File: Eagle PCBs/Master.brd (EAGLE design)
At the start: 56.8 x 35.6 mm, 9 parts

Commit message: Master PCB WIP
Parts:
- moved R1 27.9 mm to (26.7, 11.4), turned to 90 degrees
- moved C3 26.2 mm to (29.2, 2.54), turned to 180 degrees
- moved RS485-MASTER 18.1 mm to (34.3, 10.2), turned to 90 degrees
- moved 5V-VRR 17.0 mm to (39.4, 26.7), turned to 270 degrees
- moved C2 11.7 mm to (25.4, 20.3), turned to 180 degrees
- moved MEGA 4.02 mm to (44.5, 10.2), turned to 90 degrees
- moved C1 2.84 mm to (24.1, 30.5), turned to 90 degrees
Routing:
- net RS485_A: track 80.0 -> 21.3 mm
- net RS485_B: track 62.0 -> 22.8 mm
- net VCC12: track 44.2 -> 30.5 mm
- net VCC: track 39.8 -> 41.6 mm
- net GND: track 4.16 -> 4.72 mm
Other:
- board size 56.8 x 35.6 mm -> 53 x 35.6 mm

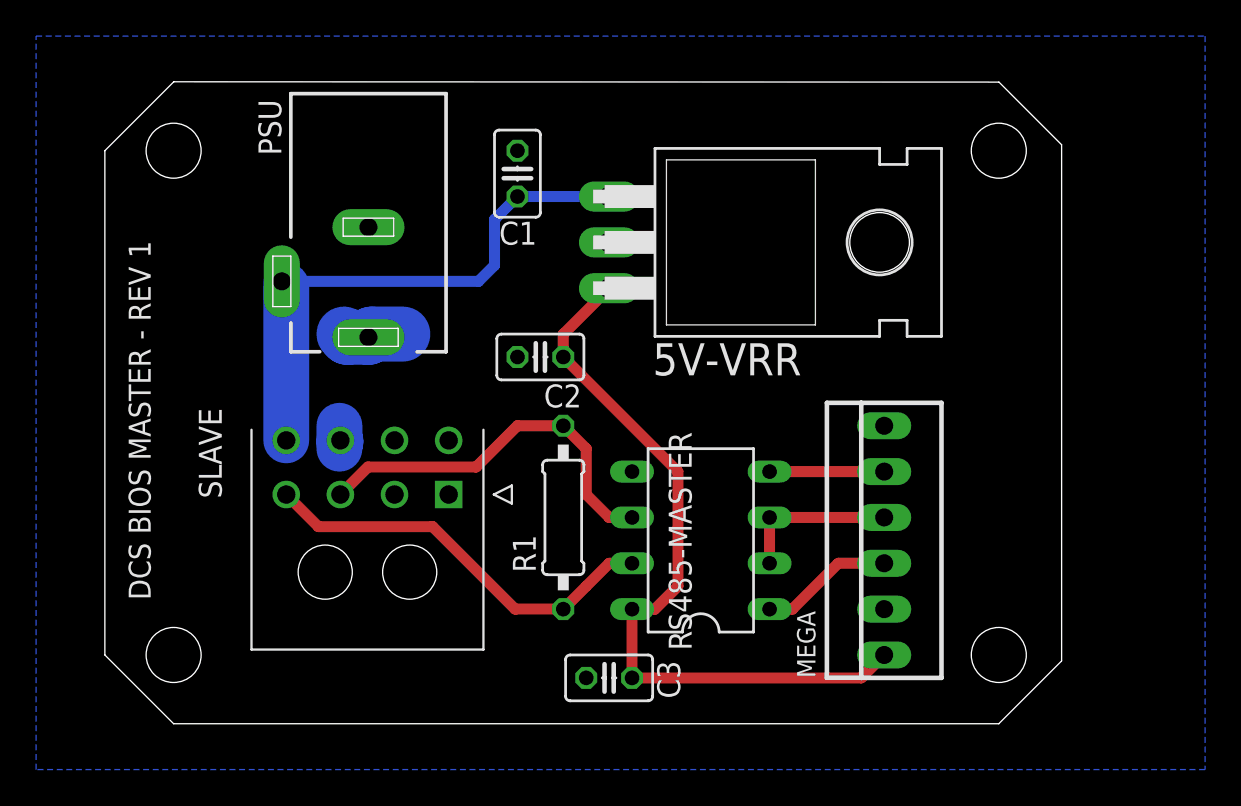
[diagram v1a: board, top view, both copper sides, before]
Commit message: Updated DC Barrel Jack
DC-044A
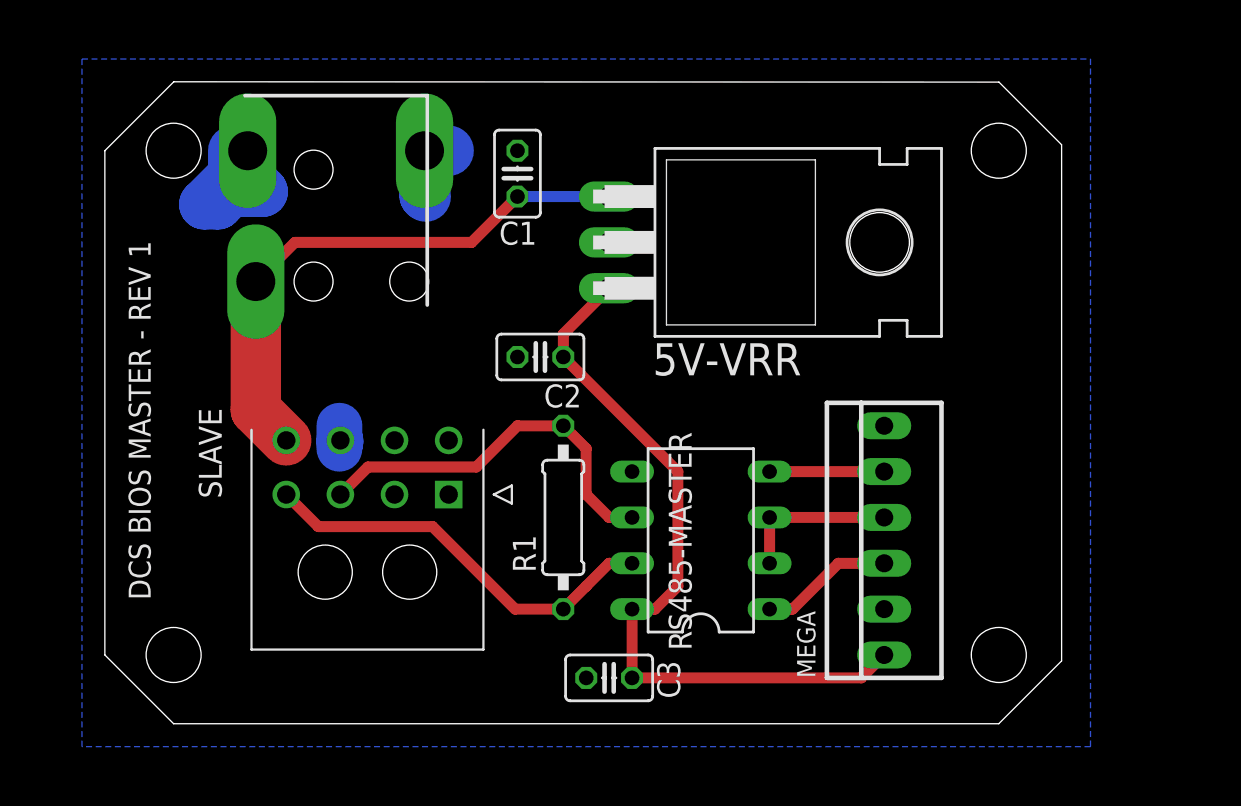
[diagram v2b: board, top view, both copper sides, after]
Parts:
- removed PSU: 12VDC C+, con-jack:DCJ0202
- added U$1: DC-044A, A10 Library:DC-044A
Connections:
- net GND: now also U$1.GND, U$1.GND-2; no longer PSU.1
- net VCC12: now also U$1.1; no longer PSU.2
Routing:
- net GND: track 4.72 -> 15.0 mm
- net VCC12: track 30.5 -> 31.0 mm
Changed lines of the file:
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@@
 <attribute name="VALUE" x="36.195" y="5.334" size="1.27" layer="27" ratio="10" rot="R90"/>
-</element>
-<element name="PSU" library="con-jack" library_urn="urn:adsk.eagle:library:154" package="DCJ0202" package3d_urn="urn:adsk.eagle:package:7491/1" value="12VDC C+" x="15.875" y="24.511" smashed="yes" rot="R180">
-<attribute name="MF" value="" x="-3.175" y="35.941" size="1.778" layer="27" rot="R180" display="off"/>
-<attribute name="MPN" value="" x="-3.175" y="35.941" size="1.778" layer="27" rot="R180" display="off"/>
-<attribute name="NAME" x="11.049" y="31.496" size="1.27" layer="25" rot="R90"/>
-<attribute name="OC_FARNELL" value="unknown" x="-3.175" y="35.941" size="1.778" layer="27" rot="R180" display="off"/>
-<attribute name="OC_NEWARK" value="unknown" x="-3.175" y="35.941" size="1.778" layer="27" rot="R180" display="off"/>
-<attribute name="POPULARITY" value="17" x="-3.175" y="35.941" size="1.778" layer="27" rot="R180" display="off"/>
-<attribute name="VALUE" x="20.574" y="35.179" size="1.27" layer="27" rot="R270"/>
 </element>
 <element name="MEGA" library="con-molex" library_urn="urn:adsk.eagle:library:165" package="22-23-2061" package3d_urn="urn:adsk.eagle:package:8078637/1" value="" x="44.45" y="10.16" smashed="yes" rot="R90">
@@
 <attribute name="VALUE" x="27.305" y="9.1694" size="1.27" layer="27" ratio="10" rot="R90"/>
 </element>
+<element name="U$1" library="A10 Library" package="DC-044A" value="DC-044A" x="14.053" y="28.28" smashed="yes" rot="R180">
+<attribute name="VALUE" x="19.133" y="22.819" size="1.27" layer="27" rot="R180"/>
+</element>
 </elements>
 <signals>
@@
 <contactref element="C1" pad="2"/>
 <contactref element="MEGA" pad="2"/>
-<contactref element="PSU" pad="1"/>
 <contactref element="C2" pad="2"/>
 <contactref element="C3" pad="2"/>
 <contactref element="SLAVE" pad="7"/>
 <polygon width="0.6096" layer="16" spacing="0.4064" isolate="0.4064">
-<vertex x="-2.54" y="38.1"/>
-<vertex x="62.23" y="38.1"/>
-<vertex x="62.23" y="-2.54"/>
-<vertex x="-2.54" y="-2.54"/>
+<vertex x="0" y="36.83"/>
+<vertex x="55.88" y="36.83"/>
+<vertex x="55.88" y="-1.27"/>
+<vertex x="0" y="-1.27"/>
 </polygon>
 <contactref element="RS485-MASTER" pad="5"/>
-<wire x1="15.875" y1="21.411" x2="16.054" y2="21.59" width="3.048" layer="16"/>
-<wire x1="16.054" y1="21.59" x2="17.78" y2="21.59" width="3.048" layer="16"/>
-<wire x1="15.875" y1="21.411" x2="14.6994" y2="21.411" width="3.048" layer="16"/>
-<wire x1="14.6994" y1="21.411" x2="14.5204" y2="21.59" width="3.048" layer="16"/>
 <wire x1="14.32" y1="15.7" x2="14.2664" y2="15.7536" width="2.54" layer="16"/>
 <wire x1="14.2664" y1="15.7536" x2="14.2664" y2="16.51" width="2.54" layer="16"/>
@@
 <wire x1="14.32" y1="15.59" x2="14.2664" y2="15.5364" width="2.54" layer="16"/>
 <wire x1="14.2664" y1="15.5364" x2="14.2664" y2="15.24" width="2.54" layer="16"/>
+<contactref element="U$1" pad="GND"/>
+<contactref element="U$1" pad="GND-2"/>
+<wire x1="18.983" y1="31.75" x2="20.32" y2="31.75" width="2.794" layer="16"/>
+<wire x1="18.983" y1="31.75" x2="18.983" y2="29.277" width="2.794" layer="16"/>
+<wire x1="18.983" y1="29.277" x2="19.05" y2="29.21" width="2.794" layer="16"/>
+<wire x1="9.183" y1="31.75" x2="9.183" y2="30.30888125" width="2.794" layer="16"/>
+<wire x1="9.183" y1="30.30888125" x2="10.01348125" y2="29.4784" width="2.794" layer="16"/>
+<wire x1="10.01348125" y1="29.4784" x2="8.2284375" y2="29.4784" width="2.794" layer="16"/>
+<wire x1="8.2284375" y1="29.4784" x2="7.53016875" y2="28.78013125" width="2.794" layer="16"/>
+<wire x1="7.53016875" y1="28.78013125" x2="6.77986875" y2="28.78013125" width="2.794" layer="16"/>
+<wire x1="6.77986875" y1="28.78013125" x2="8.382" y2="30.3822625" width="2.794" layer="16"/>
+<wire x1="8.382" y1="30.3822625" x2="8.382" y2="31.75" width="2.794" layer="16"/>
 </signal>
 <signal name="VCC12">
 <contactref element="5V-VRR" pad="1"/>
 <contactref element="C1" pad="1"/>
-<contactref element="PSU" pad="2"/>
 <wire x1="29.21" y1="29.21" x2="24.13" y2="29.21" width="0.6096" layer="16"/>
-<wire x1="24.13" y1="29.21" x2="22.86" y2="27.94" width="0.6096" layer="16"/>
-<wire x1="22.86" y1="27.94" x2="22.86" y2="25.4" width="0.6096" layer="16"/>
-<wire x1="22.86" y1="25.4" x2="21.971" y2="24.511" width="0.6096" layer="16"/>
-<wire x1="21.971" y1="24.511" x2="11.075" y2="24.511" width="0.6096" layer="16"/>
 <contactref element="SLAVE" pad="8"/>
-<wire x1="11.32" y1="24.266" x2="11.32" y2="15.7" width="2.54" layer="16"/>
-<wire x1="11.075" y1="24.511" x2="11.32" y2="24.266" width="2.032" layer="16"/>
+<contactref element="U$1" pad="1"/>
+<wire x1="9.633" y1="24.5" x2="9.633" y2="17.387" width="2.794" layer="1"/>
+<wire x1="9.633" y1="17.387" x2="11.32" y2="15.7" width="2.794" layer="1"/>
+<wire x1="9.633" y1="24.5" x2="11.803" y2="26.67" width="0.6096" layer="1"/>
+<wire x1="11.803" y1="26.67" x2="21.59" y2="26.67" width="0.6096" layer="1"/>
+<wire x1="21.59" y1="26.67" x2="24.13" y2="29.21" width="0.6096" layer="1"/>
 </signal>
 <signal name="MEGA_P2">
